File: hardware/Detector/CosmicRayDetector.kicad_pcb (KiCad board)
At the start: 2 copper layers, 100 x 70 mm, 29 parts, among them J1 USB_B_Micro, J2 Conn_01x01_Female, J3 Conn_01x01_Female, J4 Conn_01x01_Female, J5 Conn_01x01_Female, J6 Conn_01x04, J7 Conn_01x02, U1 HEF4093B

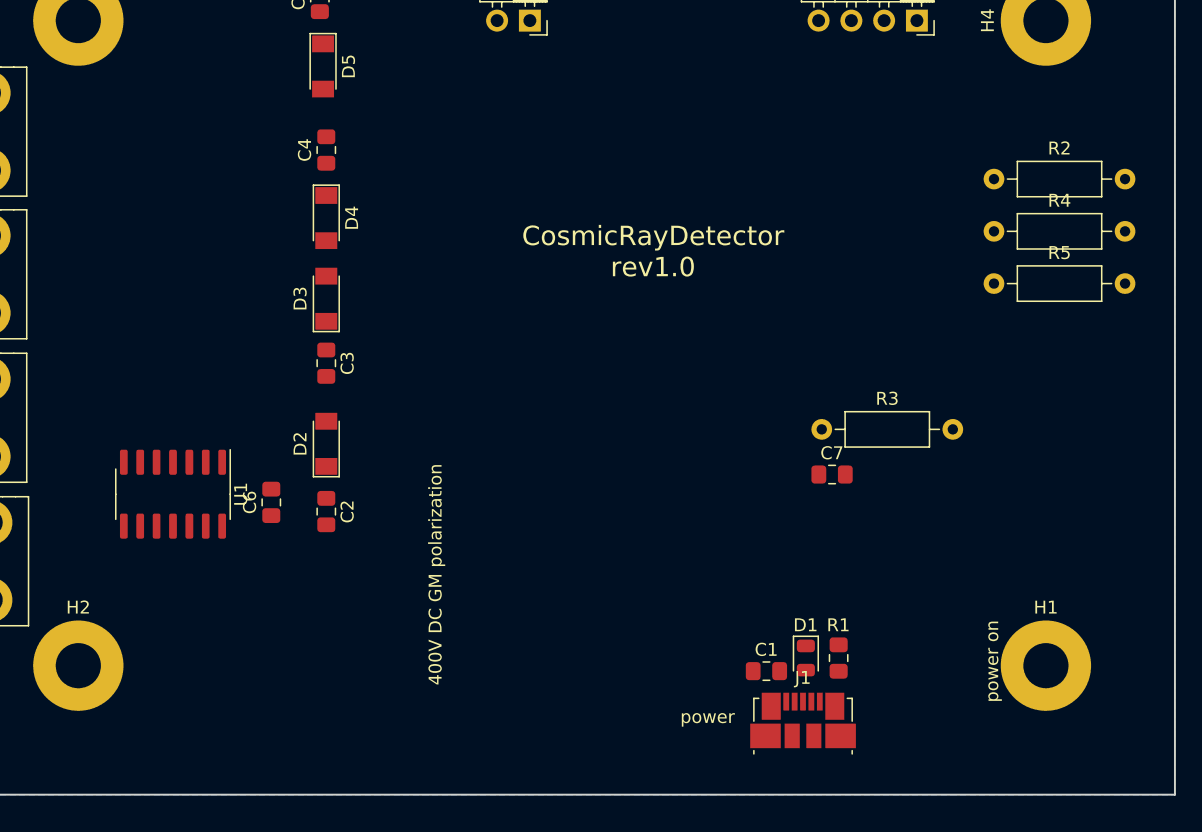
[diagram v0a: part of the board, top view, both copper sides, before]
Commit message: added li-ion charger
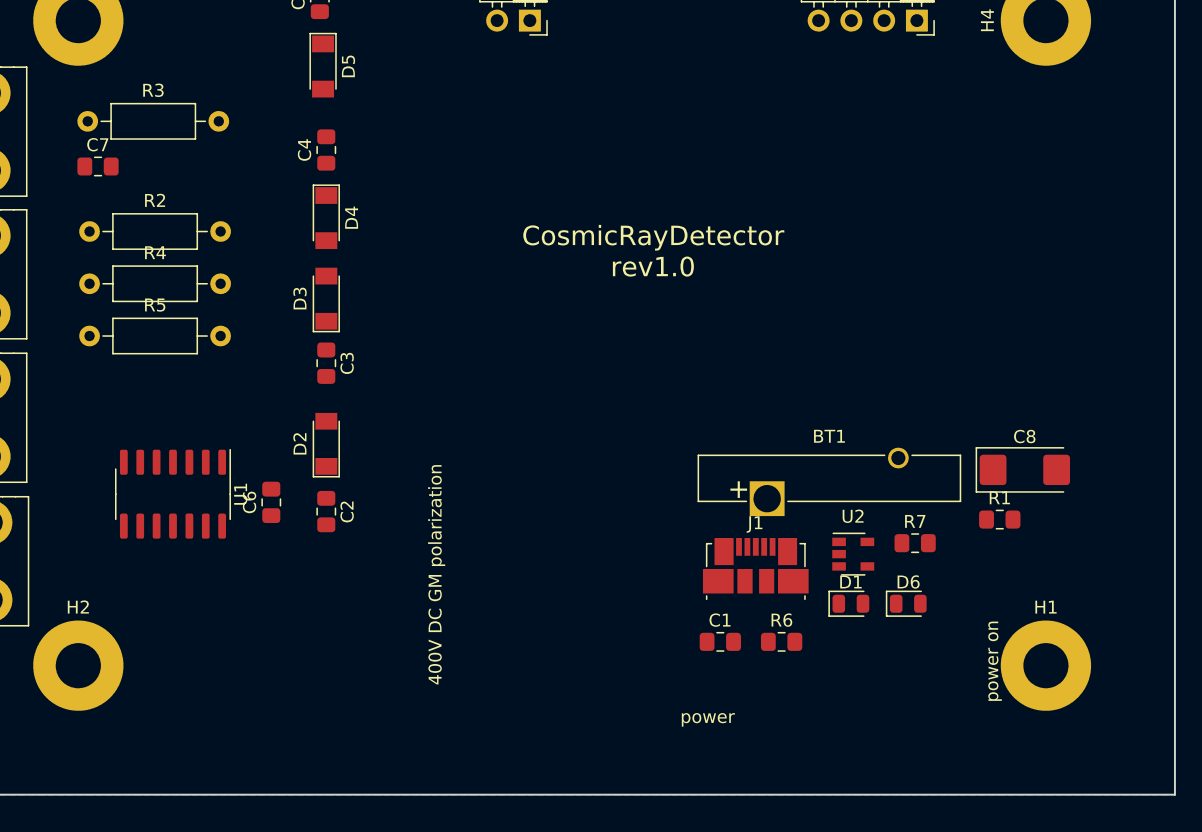
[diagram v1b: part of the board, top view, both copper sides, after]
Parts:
- added BT1: Battery_Cell, Battery:Battery_Panasonic_CR2025-V1AK_Vertical_CircularHoles, F.Cu at (88.4, 67.1)
- added C8: 10u, Capacitor_Tantalum_SMD:CP_EIA-6032-28_Kemet-C, F.Cu at (108.4, 64.8)
- added D6: red, LED_SMD:LED_0805_2012Metric, F.Cu at (99.3, 75.2)
- added R6: 2k2, Resistor_SMD:R_0805_2012Metric_Pad1.15x1.40mm_HandSolder, F.Cu at (89.5, 78.2)
- added R7: 470R, Resistor_SMD:R_0805_2012Metric_Pad1.15x1.40mm_HandSolder, F.Cu at (99.9, 70.5)
- added U2: MCP73831-5-OT, Package_TO_SOT_SMD:SOT-23-5, F.Cu at (95.1, 71.4)
- moved R2 70.2 mm to (35.9, 46.3)
- moved R4 70.2 mm to (35.9, 50.4)
- moved R5 70.2 mm to (35.9, 54.4)
- moved C7 61.7 mm to (36.5, 41.3)
- moved R3 61.7 mm to (35.7, 37.8)
- moved R1 16.5 mm to (106.4, 68.7), turned to 0 degrees
- moved J1 12.5 mm to (87.5, 72.3)
- moved D1 5.47 mm to (94.9, 75.2), turned to 0 degrees
- moved C1 4.23 mm to (84.8, 78.2)
